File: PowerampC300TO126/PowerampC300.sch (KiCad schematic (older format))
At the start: 110 parts, among them J1 Conn_01x02, J2 Conn_01x02, J3 Conn_01x02, J4 Conn_01x01, J5 Conn_01x01, J6 Conn_01x01, J7 Conn_01x01, J8 Conn_01x02, J9 Conn_Coaxial, Q1 2N5551, Q10 MJE350, Q11 MJE340, Q12 MJE340, Q13 2N5551, Q14 2N5401, Q15 MJE340, Q16 MJE350, Q17 MJL3281A, Q18 MJL1302A, Q19 MJL3281A, Q2 2N5551, Q20 MJL1302A, Q21 MJL3281A, Q22 MJL1302A, Q23 MJL3281A, Q24 MJL1302A, Q3 2N5401, Q4 2N5401, Q5 2N5551, Q6 2N5551, Q7 2N5551, Q8 2N5401

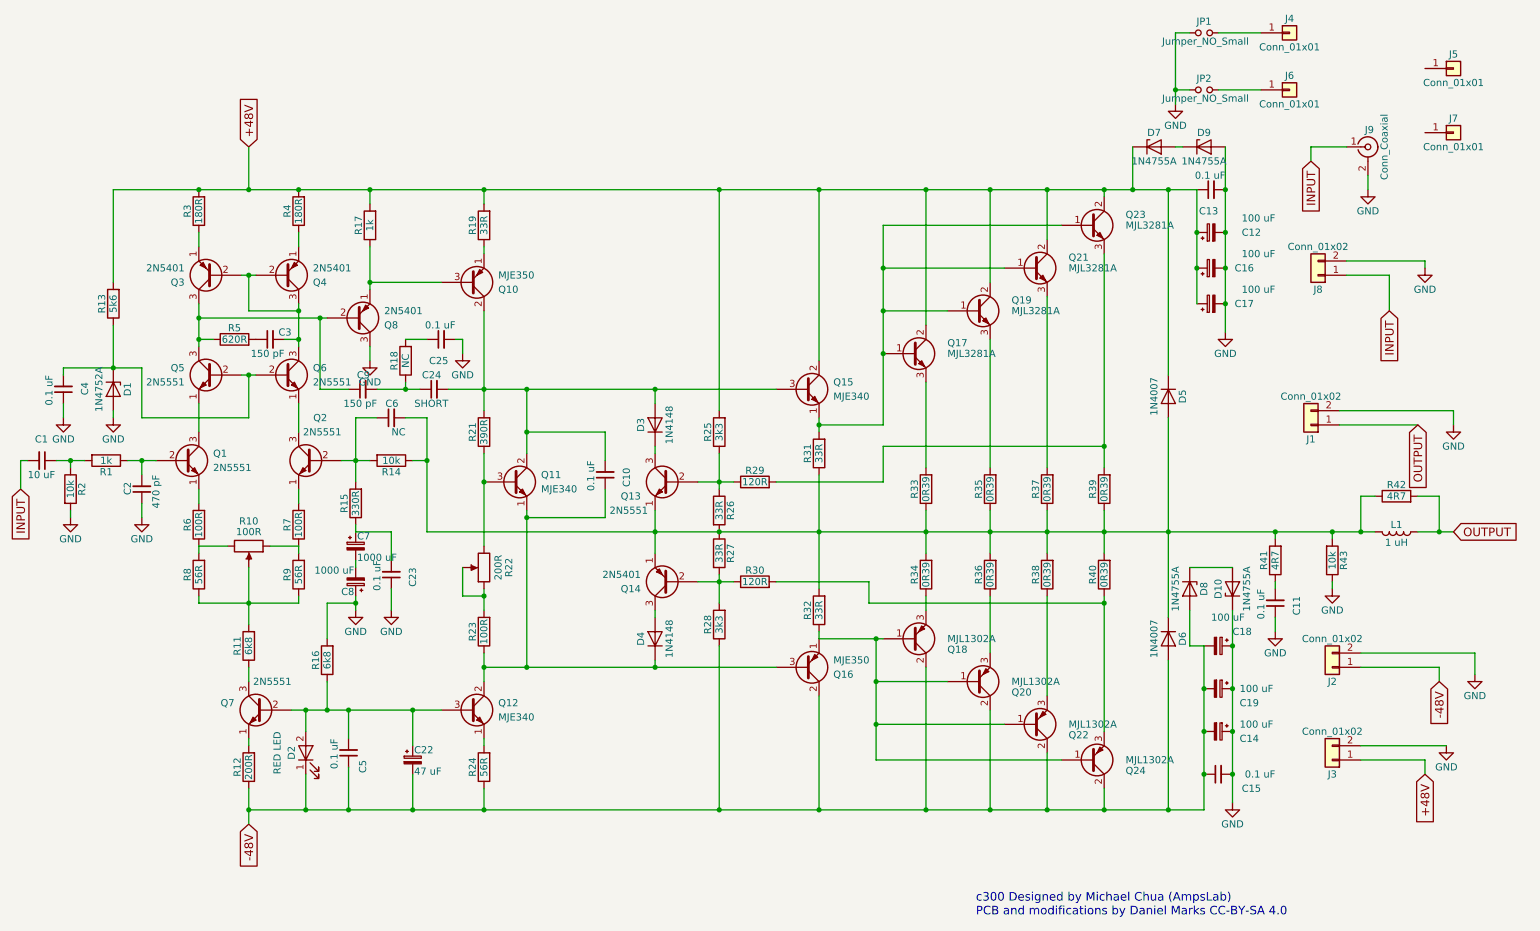
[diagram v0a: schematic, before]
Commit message: Moved Q1 and Q2 together
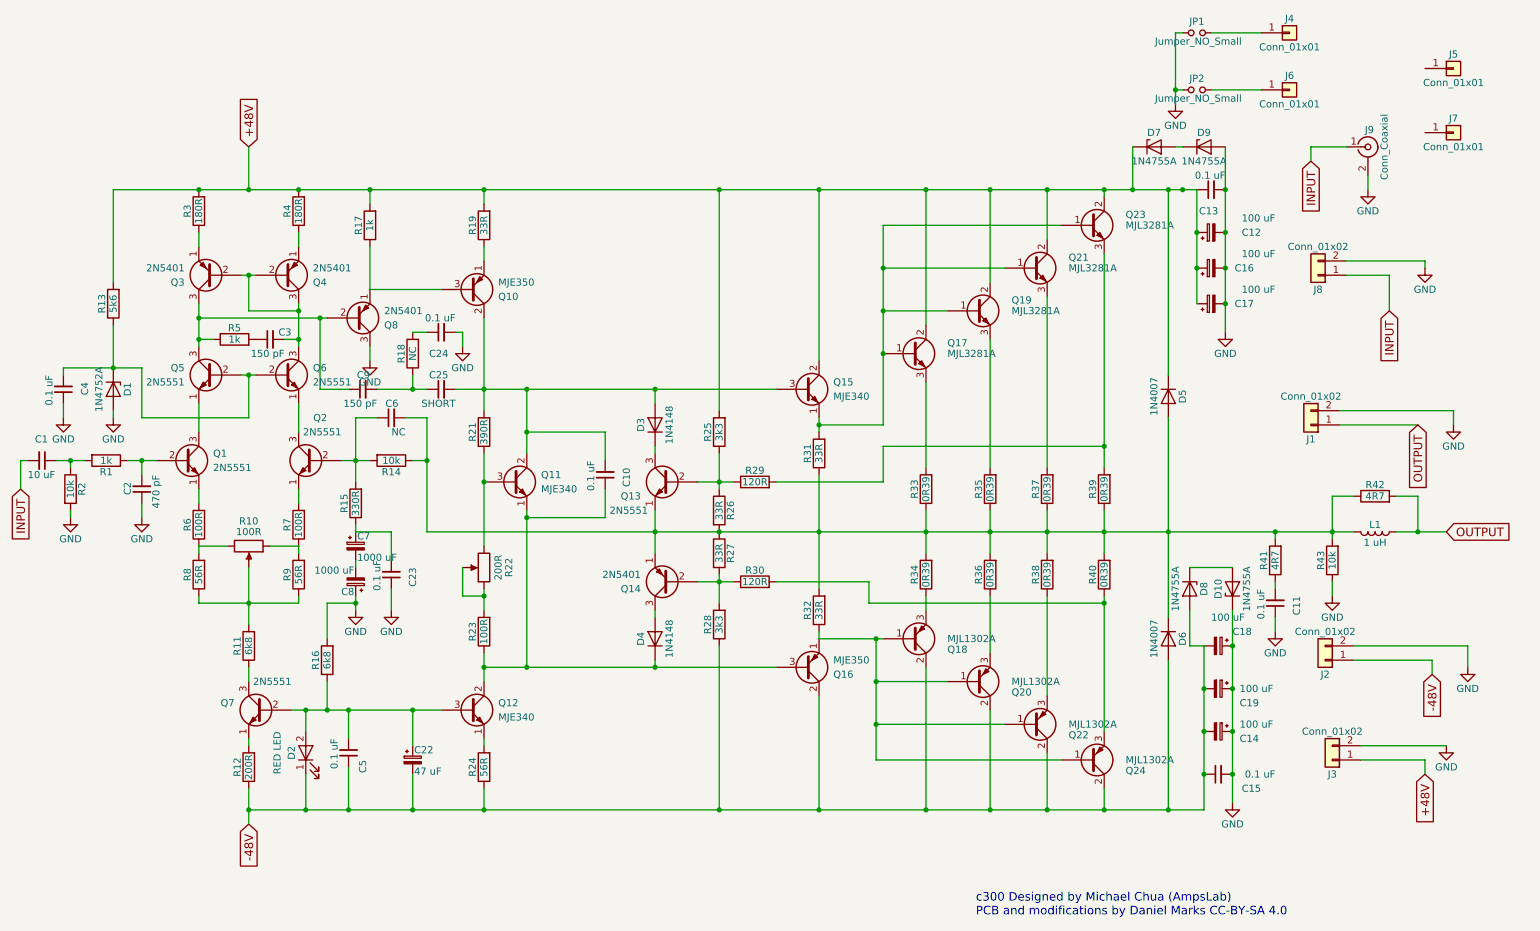
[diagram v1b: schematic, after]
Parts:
- C24: value SHORT -> 0.1 uF; footprint Capacitors_THT:C_Disc_D5.0mm_W2.5mm_P5.00mm -> Capacitors_THT:C_Axial_L3.8mm_D2.6mm_P10.00mm_Horizontal; LCSC C366798 -> C390130
- C25: value 0.1 uF -> SHORT; footprint Capacitors_THT:C_Axial_L3.8mm_D2.6mm_P10.00mm_Horizontal -> Capacitors_THT:C_Disc_D5.0mm_W2.5mm_P5.00mm; LCSC C390130 -> C366798
- R18: LCSC C57436 -> C173010
- R5: value 620R -> 1k
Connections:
- net GND: now also C24.2; no longer C25.2
- net at C9.2, R18.1: now also C25.1; no longer C24.1
- net at C10.2, D3.2 (A), Q10.2 (C)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: now also C25.2; no longer C24.2
- net at R18.2: now also C24.1; no longer C25.1
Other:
- moved on the sheet: J2, L1, R42

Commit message: Added option for spade terminal power connections
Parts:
- J1, J2, J3: footprint Connectors_Terminal_Blocks:TerminalBlock_bornier-2_P5.08mm -> poweramp:TerminalBlock_bornier-2_P5.08mm_with_spade
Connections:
- net -48V: now also J2.2 (Pin_2); no longer J2.1 (Pin_1)
- net GND: now also J2.1 (Pin_1); no longer J2.2 (Pin_2)
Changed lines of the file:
@@
 F 0 "J1" H 9700 3550 50  0000 C CNN
 F 1 "Conn_01x02" H 9700 3250 50  0000 C CNN
-F 2 "Connectors_Terminal_Blocks:TerminalBlock_bornier-2_P5.08mm" H 9700 3450 50  0001 C CNN
+F 2 "poweramp:TerminalBlock_bornier-2_P5.08mm_with_spade" H 9700 3450 50  0001 C CNN
 F 3 "" H 9700 3450 50  0001 C CNN
 F 4 "C395849" H 9700 3450 60  0001 C CNN "LCSC"
@@
 L Conn_01x02 J2
 U 1 1 5F3DAA81
-P 9800 5100
-F 0 "J2" H 9800 5200 50  0000 C CNN
-F 1 "Conn_01x02" H 9800 4900 50  0000 C CNN
-F 2 "Connectors_Terminal_Blocks:TerminalBlock_bornier-2_P5.08mm" H 9800 5100 50  0001 C CNN
-F 3 "" H 9800 5100 50  0001 C CNN
-F 4 "C395849" H 9800 5100 60  0001 C CNN "LCSC"
-	1    9800 5100
-	-1   0    0    1
+P 9800 5000
+F 0 "J2" H 9800 5100 50  0000 C CNN
+F 1 "Conn_01x02" H 9800 4800 50  0000 C CNN
+F 2 "poweramp:TerminalBlock_bornier-2_P5.08mm_with_spade" H 9800 5000 50  0001 C CNN
+F 3 "" H 9800 5000 50  0001 C CNN
+F 4 "C395849" H 9800 5000 60  0001 C CNN "LCSC"
+	1    9800 5000
+	-1   0    0    -1
 $EndComp
 $Comp
@@
 F 0 "J3" H 9850 5900 50  0000 C CNN
 F 1 "Conn_01x02" H 9850 5600 50  0000 C CNN
-F 2 "Connectors_Terminal_Blocks:TerminalBlock_bornier-2_P5.08mm" H 9850 5800 50  0001 C CNN
+F 2 "poweramp:TerminalBlock_bornier-2_P5.08mm_with_spade" H 9850 5800 50  0001 C CNN
 F 3 "" H 9850 5800 50  0001 C CNN
 F 4 "C395849" H 9850 5800 60  0001 C CNN "LCSC"

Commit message: Added OITPC compensation
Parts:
- added C20: NC, Capacitors_THT:C_Disc_D5.0mm_W2.5mm_P5.00mm, symbol C_Small
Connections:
- net at C9.1, Q3.3 (C), Q5.3 (C)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: now also C20.1
- net at C6.2, D5.2 (A), D6.1 (K)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: now also C20.2
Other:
- moved on the sheet: C24, C25, C6, C9, R14, R18

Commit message: Redid star scheme again, added grounding diagram, modified drill template
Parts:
- added D11, D12: 1N4148, Diodes_THT:D_DO-35_SOD27_P7.62mm_Horizontal, symbol D
- added R20: 10R, Resistors_THT:R_Axial_DIN0207_L6.3mm_D2.5mm_P7.62mm_Horizontal, symbol R
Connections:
- net GND: now also D11.2 (A), D12.1 (K), R20.2; no longer C2.1, C23.1, C24.2, C4.1, C8.1, D1.2 (A), J8.2 (Pin_2), J9.2 (Ext), JP2.1, Q8.3 (C), R16.2, R2.2
- new net GNDS: C2.1, C23.1, C24.2, C4.1, C8.1, D1.2 (A), D11.1 (K), D12.2 (A), J8.2 (Pin_2), J9.2 (Ext), JP2.1, Q8.3 (C), R16.2, R2.2, R20.1
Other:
- moved on the sheet: C25, C6

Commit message: Changed components for lower quiescent power
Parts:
- R24: value 56R -> 120R
- R25, R28: value 3k3 -> 6k8
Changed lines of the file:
@@
 P 3900 5850
 F 0 "R24" V 3980 5850 50  0000 C CNN
-F 1 "56R" V 3900 5850 50  0000 C CNN
+F 1 "120R" V 3900 5850 50  0000 C CNN
 F 2 "Resistors_THT:R_Axial_DIN0207_L6.3mm_D2.5mm_P7.62mm_Horizontal" V 3830 5850 50  0001 C CNN
 F 3 "" H 3900 5850 50  0001 C CNN
@@
 P 5550 3500
 F 0 "R25" V 5630 3500 50  0000 C CNN
-F 1 "3k3" V 5550 3500 50  0000 C CNN
+F 1 "6k8" V 5550 3500 50  0000 C CNN
 F 2 "Resistors_THT:R_Axial_DIN0411_L9.9mm_D3.6mm_P15.24mm_Horizontal" V 5480 3500 50  0001 C CNN
 F 3 "" H 5550 3500 50  0001 C CNN
@@
 P 5550 4850
 F 0 "R28" V 5630 4850 50  0000 C CNN
-F 1 "3k3" V 5550 4850 50  0000 C CNN
+F 1 "6k8" V 5550 4850 50  0000 C CNN
 F 2 "Resistors_THT:R_Axial_DIN0411_L9.9mm_D3.6mm_P15.24mm_Horizontal" V 5480 4850 50  0001 C CNN
 F 3 "" H 5550 4850 50  0001 C CNN

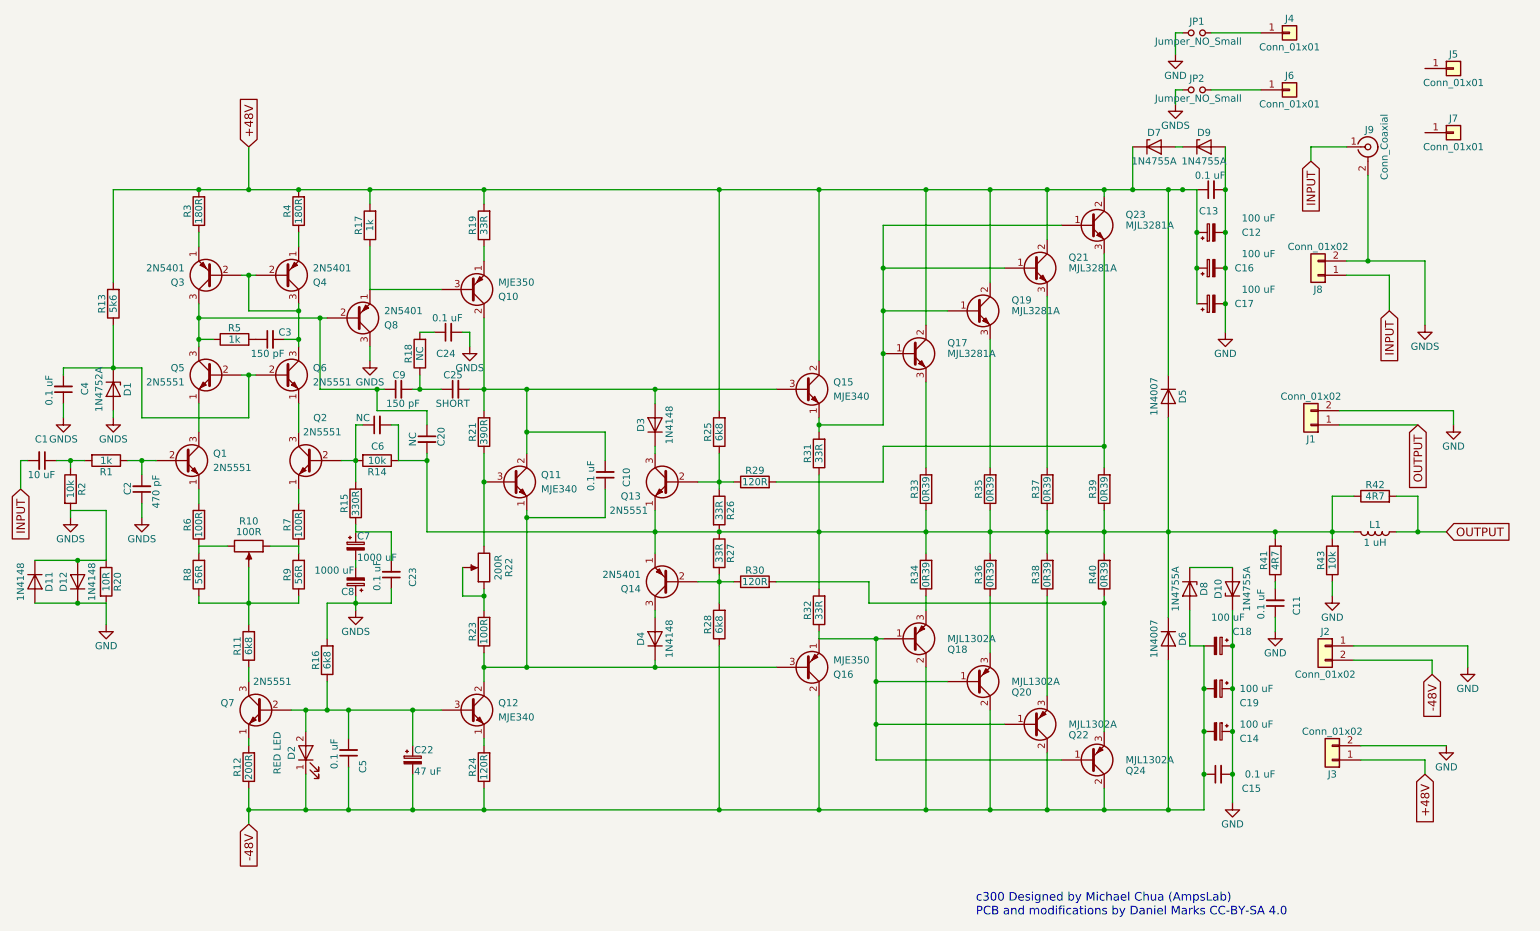
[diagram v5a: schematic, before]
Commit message: Added base stopper resistors
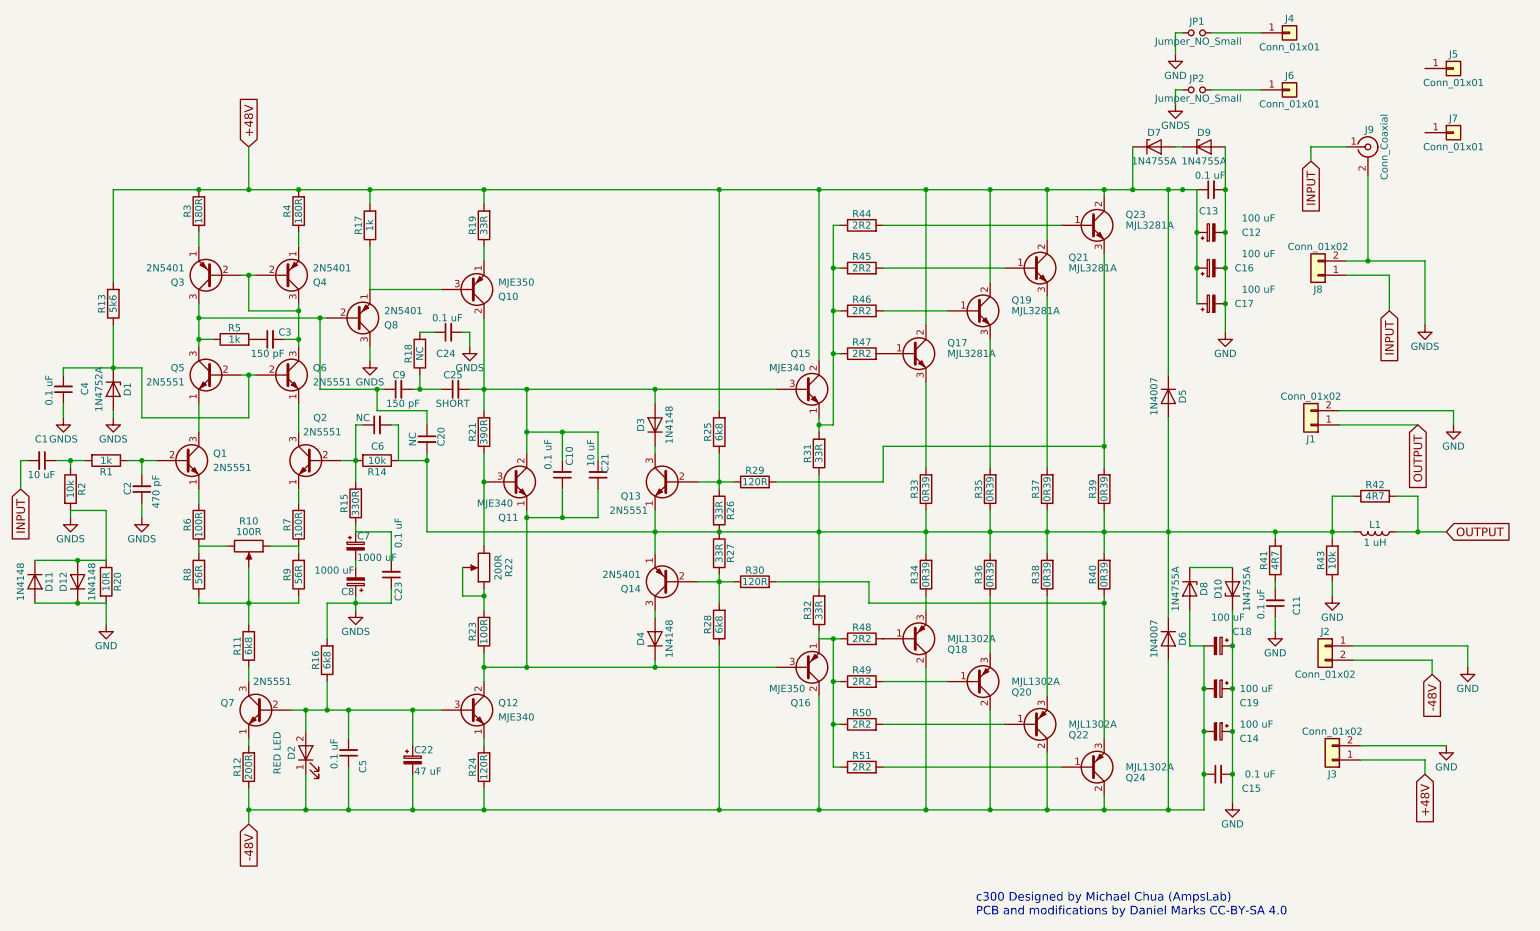
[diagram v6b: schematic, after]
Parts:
- added C21: 10 uF, Capacitors_THT:C_Disc_D5.0mm_W2.5mm_P5.00mm, symbol C_Small
- added R44, R45, R46, R47, R48, R49, R50, R51: 2R2, Resistors_THT:R_Axial_DIN0411_L9.9mm_D3.6mm_P15.24mm_Horizontal, symbol R
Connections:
- net at C10.1, D4.1 (K), Q11.1 (E)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: now also C21.1
- net at C10.2, C25.2, D3.2 (A)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: now also C21.2
- new net: Q15.1 (E), R31.2, R44.1, R45.1, R46.1, R47.1
- new net: Q16.1 (E), R32.1, R48.1, R49.1, R50.1, R51.1
- new net: Q17.1 (B), R47.2
- new net: Q18.1 (B), R48.2
- new net: Q19.1 (B), R46.2
- new net: Q21.1 (B), R45.2
- new net: Q23.1 (B), R44.2
- new net: Q20.1 (B), R49.2
- new net: Q22.1 (B), R50.2
- new net: Q24.1 (B), R51.2
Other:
- moved on the sheet: C10, Q24
